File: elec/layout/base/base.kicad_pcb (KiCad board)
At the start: 2 copper layers, 38 parts, among them U1 ?, U2 ?, U3 ?, U4 ?, U5 ?, U6 ?, U7 ?, U8 ?, U9 ?

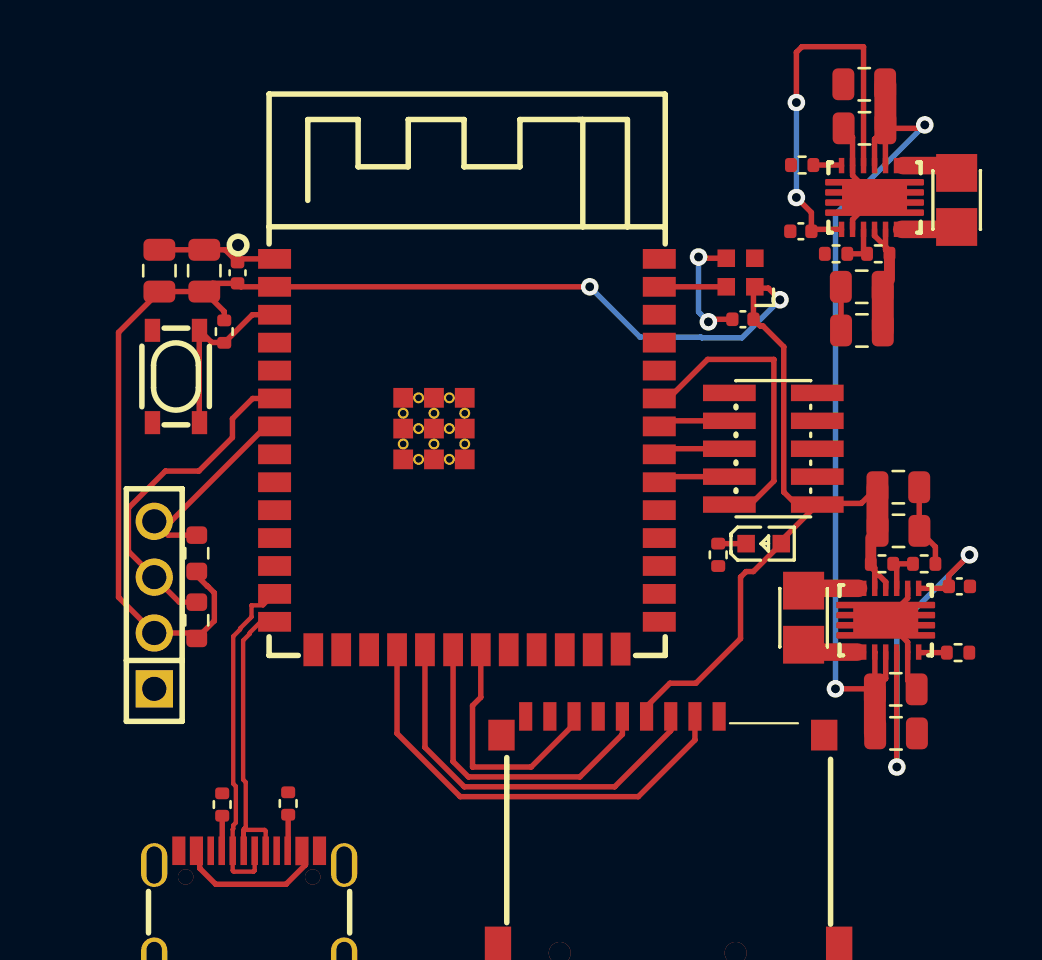
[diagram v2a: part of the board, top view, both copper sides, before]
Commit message: Update to build with the v0.3 compiler
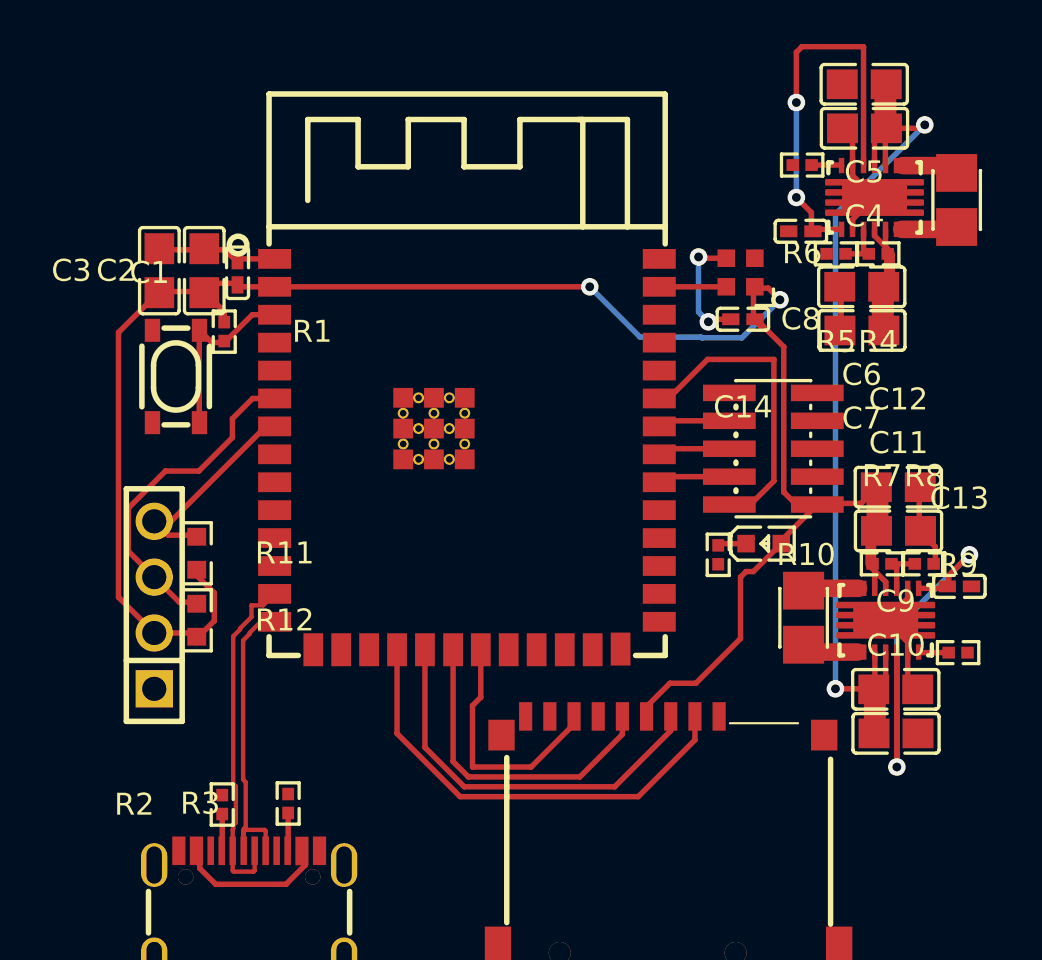
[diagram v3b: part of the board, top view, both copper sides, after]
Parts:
- C1, C13, C14, C8: value 16V 100nF X7R ±10% 0402 Multilayer Ceramic Capacitors MLCC - SMD/SMT ROHS -> 100nF ±10% 16V X7R; footprint lib:C0402 -> atopile:C0402-b3ef17
- C10, C11, C12, C2, C3, C4, C5, C6, C7, C9: value 25V 10uF X5R ±10% 0805 Multilayer Ceramic Capacitors MLCC - SMD/SMT ROHS -> 10µF ±10% 25V X5R; footprint lib:C0805 -> atopile:C0805-3b2e55
- L1, L2, LED1, U1, U2, U3, U4, U5, U6, U7, U8, U9: value ? -> (none)
- R1: value 62.5mW Thick Film Resistors 50V ±100ppm/℃ ±1% 10kΩ 0402 Chip Resistor - Surface Mount ROHS -> 10kΩ ±1% 62.5mW; footprint lib:R0402 -> atopile:R0402-56259e
- R10: value 62.5mW Thick Film Resistors 50V ±100ppm/℃ ±1% 330Ω 0402 Chip Resistor - Surface Mount ROHS -> 1kΩ ±1% 62.5mW; footprint lib:R0402 -> atopile:R0402-56259e
- R11, R12: value 100mW Thick Film Resistors 75V ±100ppm/℃ ±1% 2.7kΩ 0603 Chip Resistor - Surface Mount ROHS -> 2.7kΩ ±1% 100mW; footprint lib:R0603 -> atopile:R0603-ebcab9
- R2, R3: value 62.5mW Thick Film Resistors 50V ±100ppm/℃ ±1% 4.7kΩ 0402 Chip Resistor - Surface Mount ROHS -> 4.7kΩ ±1% 62.5mW; footprint lib:R0402 -> atopile:R0402-56259e
- R4: value 62.5mW 50V ±100ppm/℃ ±1% 25.5kΩ 0402 Chip Resistor - Surface Mount ROHS -> 1kΩ ±1% 62.5mW; footprint lib:R0402 -> atopile:R0402-56259e
- R5: value 62.5mW Thick Film Resistors 50V ±1% ±200ppm/℃ 2.8kΩ 0402 Chip Resistor - Surface Mount ROHS -> 1kΩ ±1% 62.5mW; footprint lib:R0402 -> atopile:R0402-56259e
- R6, R9: value 62.5mW Thick Film Resistors 50V ±100ppm/℃ ±1% 1MΩ 0402 Chip Resistor - Surface Mount ROHS -> 1MΩ ±1% 62.5mW; footprint lib:R0402 -> atopile:R0402-56259e
- R7: value 62.5mW Thick Film Resistors 50V ±100ppm/℃ ±1% 23.7kΩ 0402 Chip Resistor - Surface Mount ROHS -> 1kΩ ±1% 62.5mW; footprint lib:R0402 -> atopile:R0402-56259e
- R8: value 62.5mW Thick Film Resistors 50V ±100ppm/℃ ±1% 4.3kΩ 0402 Chip Resistor - Surface Mount ROHS -> 1kΩ ±1% 62.5mW; footprint lib:R0402 -> atopile:R0402-56259e
